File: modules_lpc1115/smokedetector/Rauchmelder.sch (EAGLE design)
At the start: 75 parts, among them IC1 BD9G101, IC2 LPC1115, Q1 BC856, Q3 BCP52, Q4 ASFL, T1 BC847C, T2 BC847C

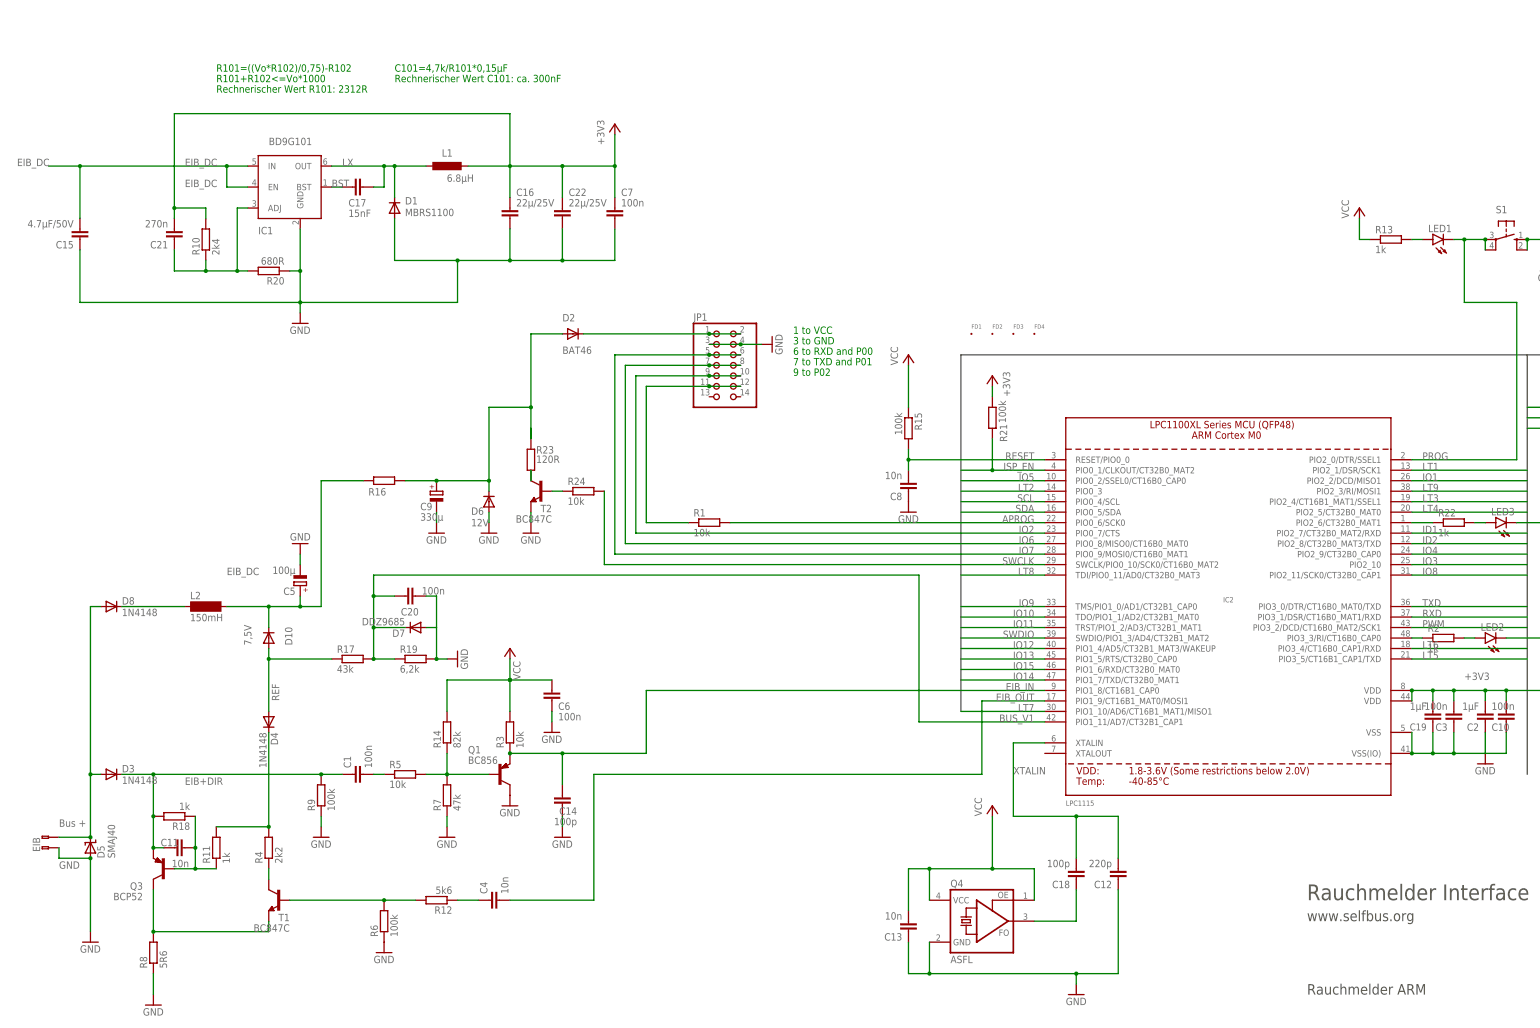
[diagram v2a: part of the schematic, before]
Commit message: [RM] - pwr mlccs changed to 2 x 47uF and adj-voltage divider 1k6/470R
- according to ROHM spec: switched to 2 x 47uF mlccs (instead of 1 x 22uF of the old design)
- according to ROHM spec: adjusted voltage divider to get 3,3V output instead of  (instead of  3,397V from the old design)
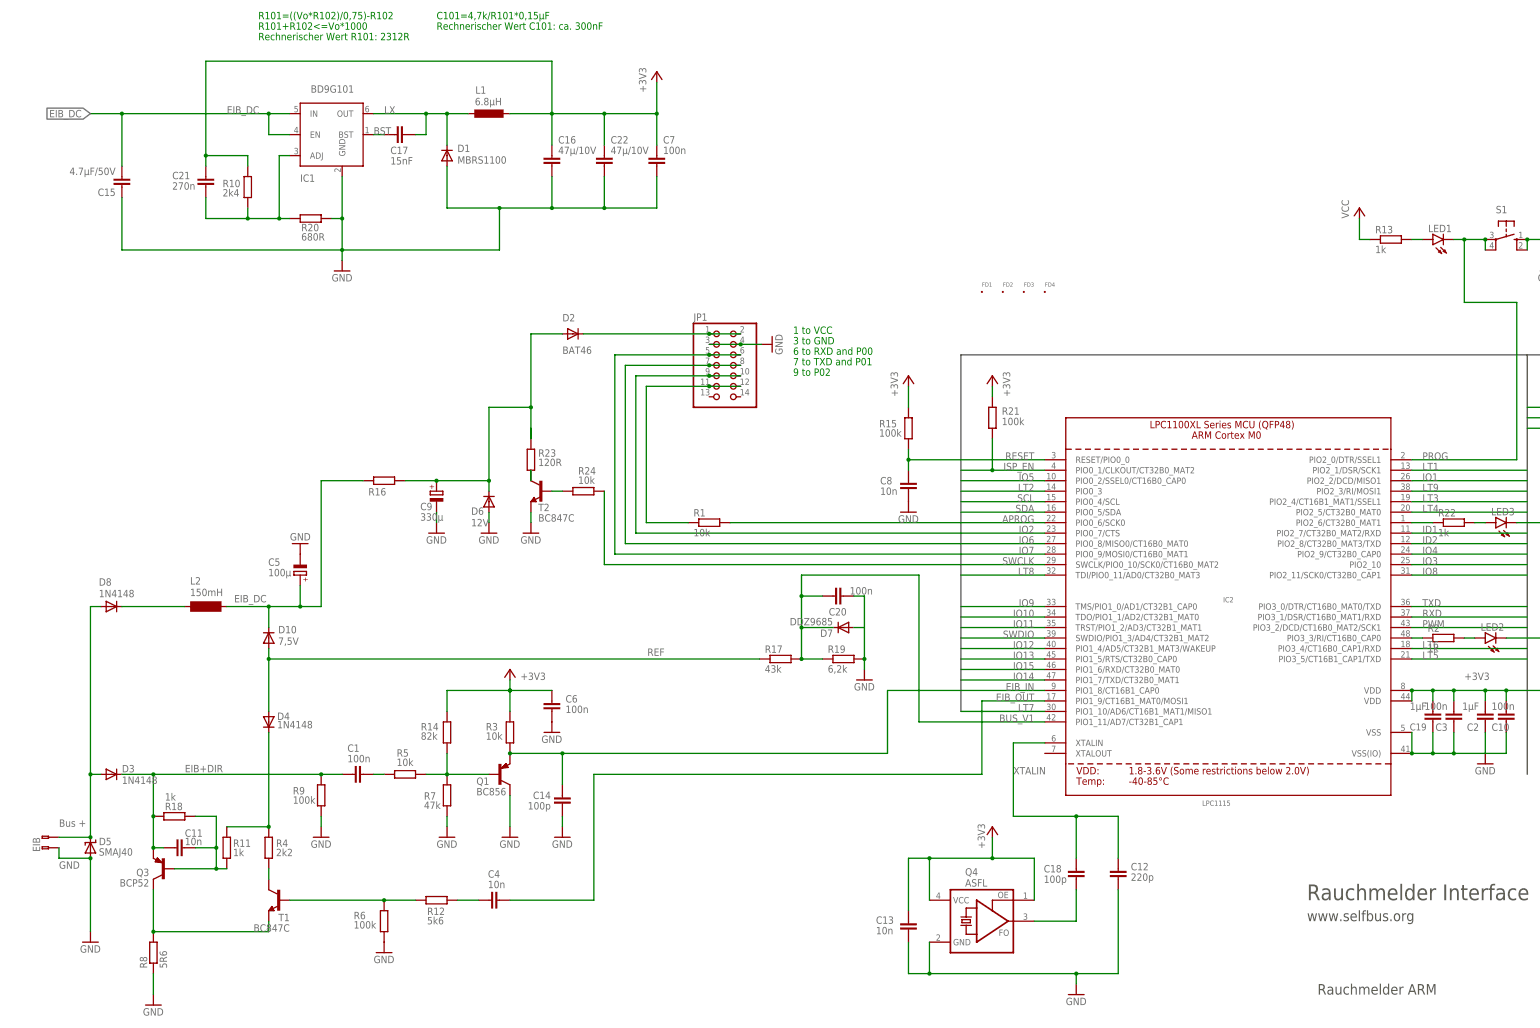
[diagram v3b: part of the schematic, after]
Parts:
- C16, C22: value 22µ/25V -> 47µ/10V
- D1: device microbuilder:DIODESMA -> microbuilder:DIODESOD-123
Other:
- moved on the sheet: C15, C16, C17, C20, C21, C22, C5, C6, C7, D1, D7, FD1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

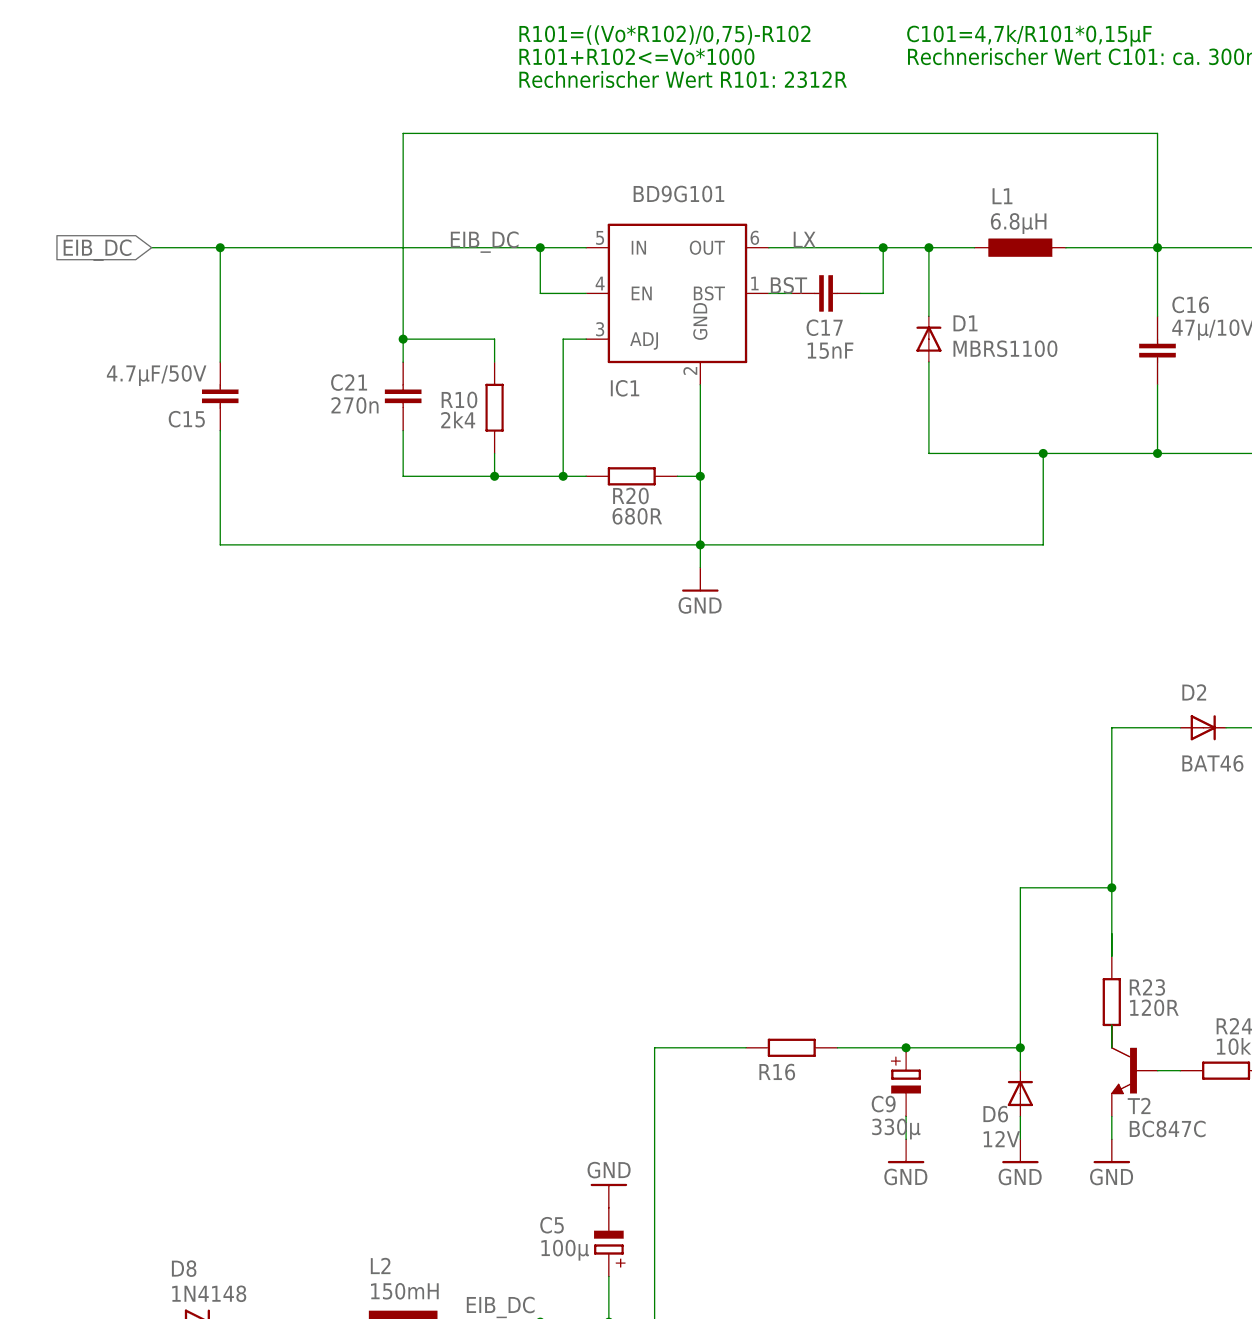
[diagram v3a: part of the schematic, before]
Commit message: [RM] - removed thermals from buck converter polygons
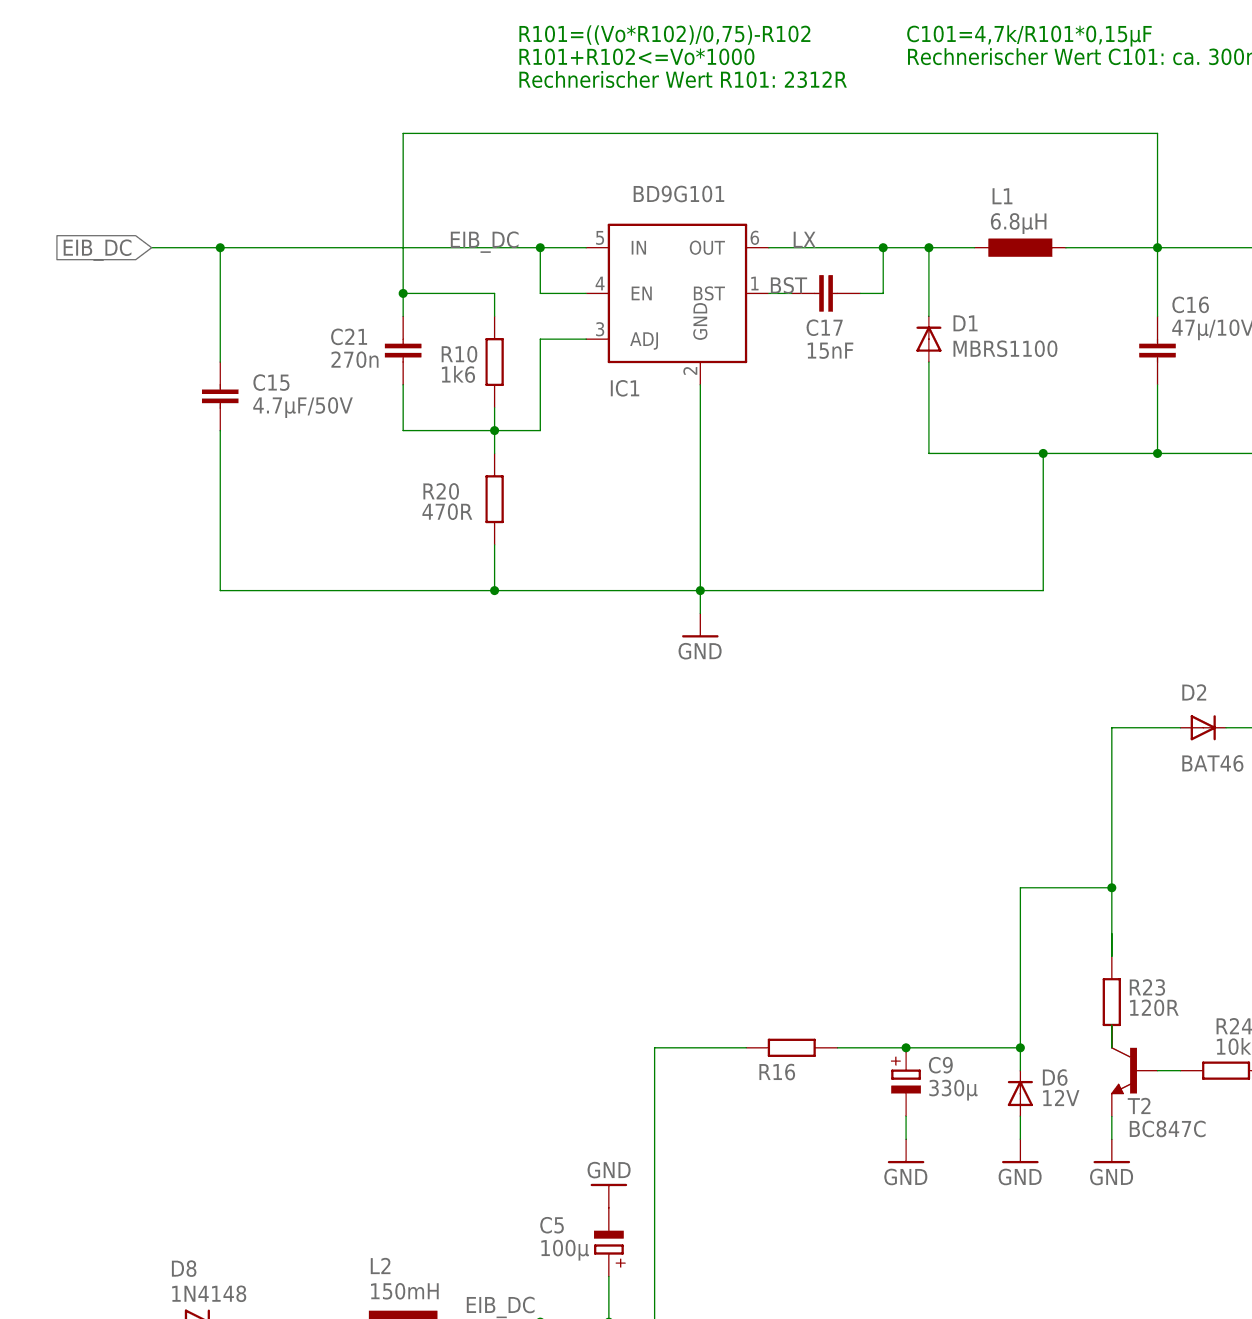
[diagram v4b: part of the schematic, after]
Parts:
- R10: value 2k4 -> 1k6
- R20: value 680R -> 470R
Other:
- moved on the sheet: C21, R10, R20

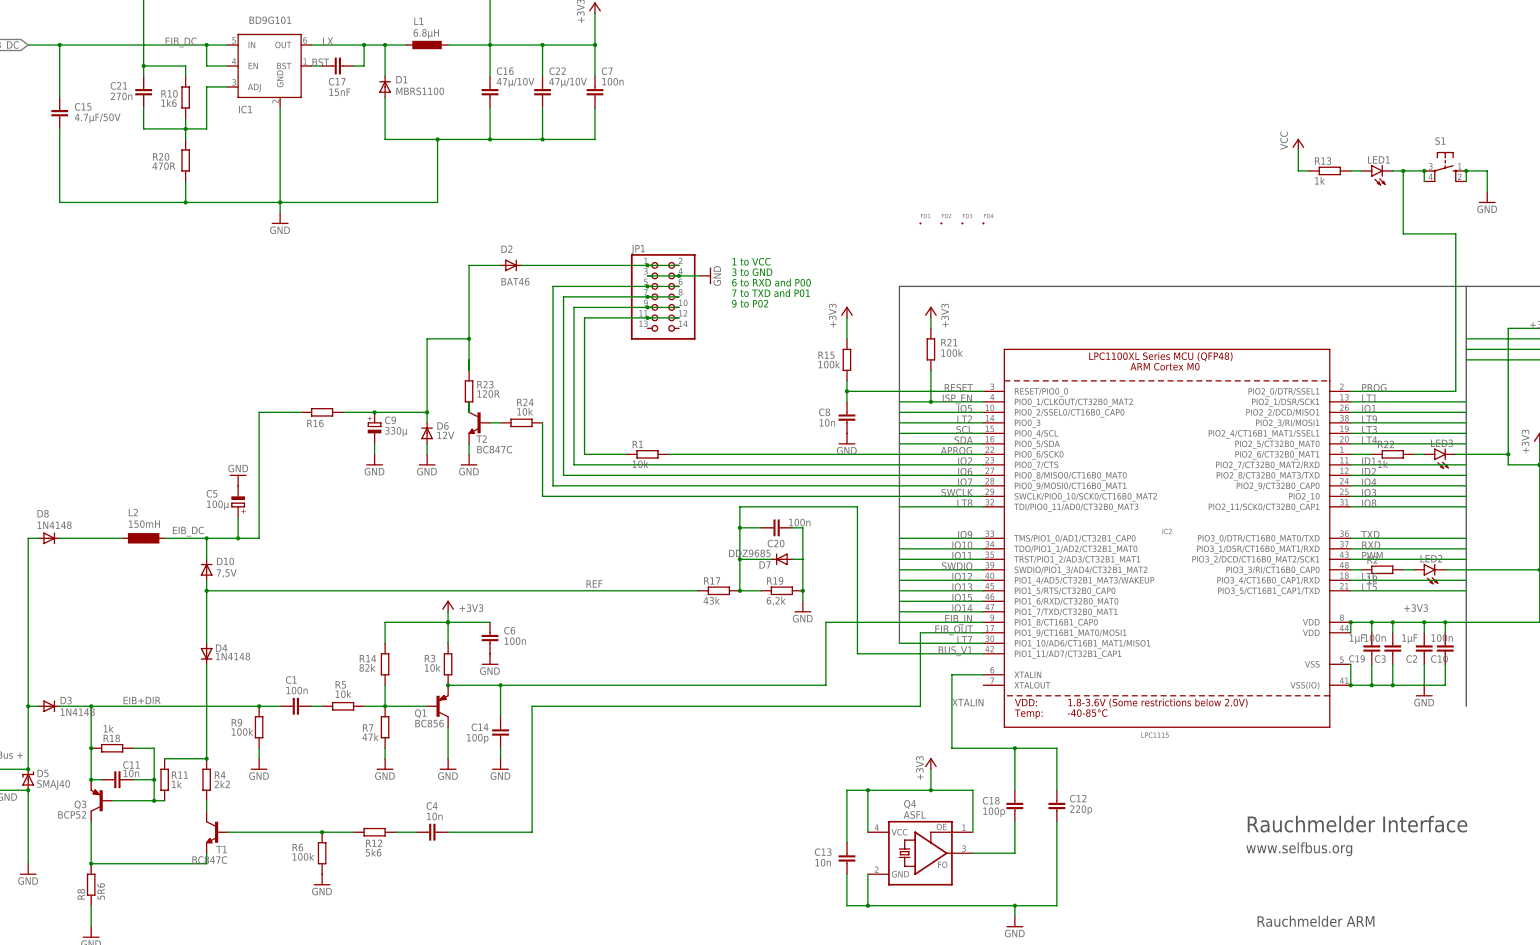
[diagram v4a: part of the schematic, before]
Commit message: [RM] - changed footprints from 1206 to 0805
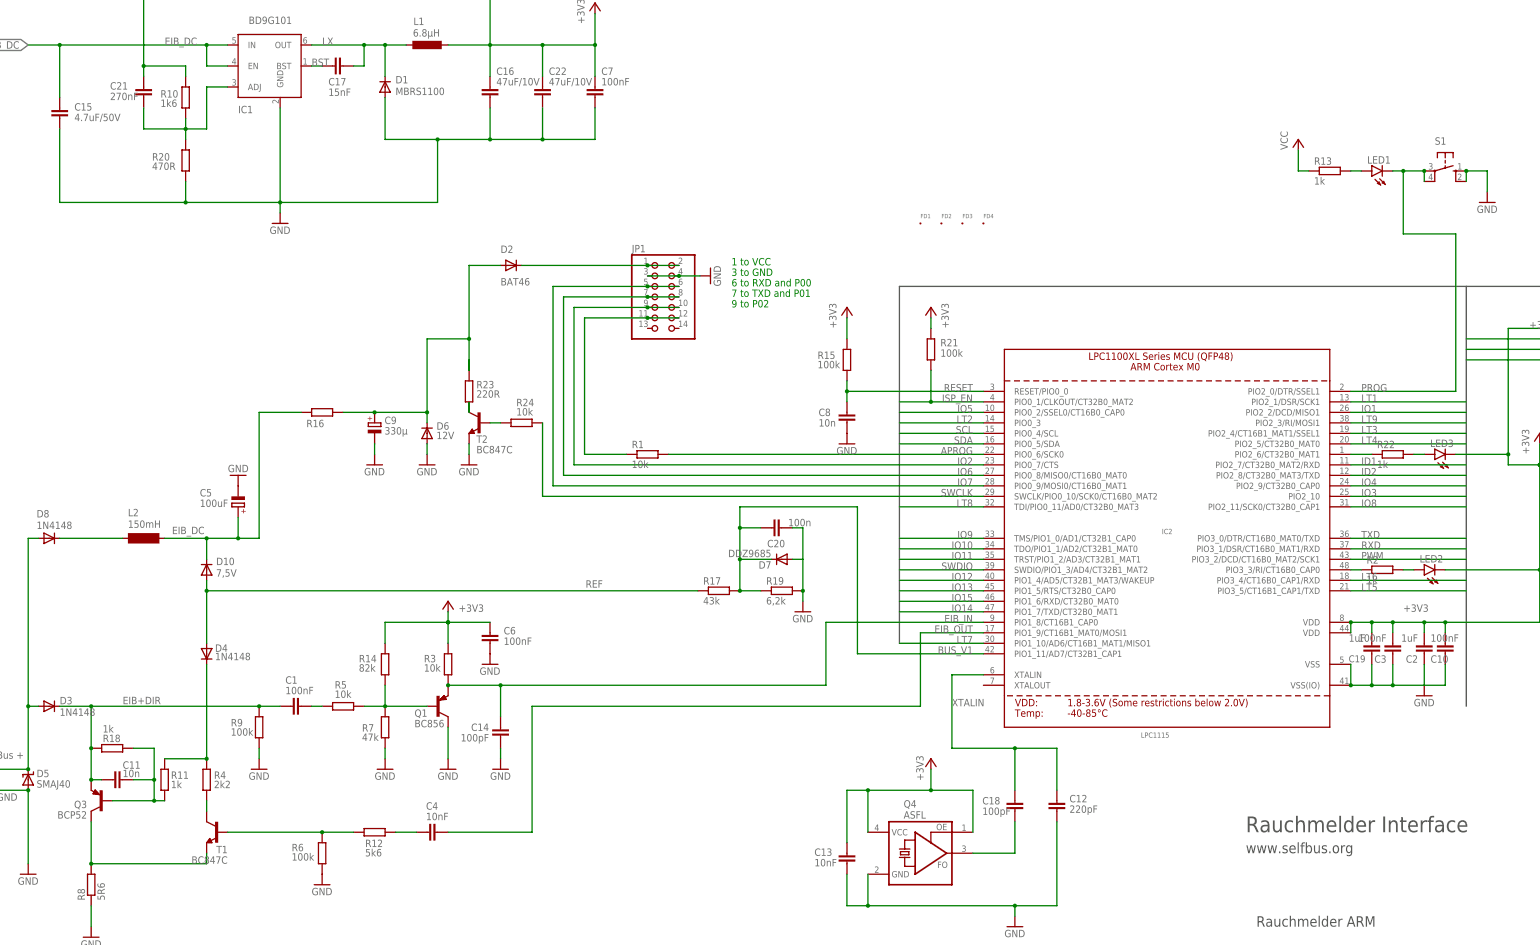
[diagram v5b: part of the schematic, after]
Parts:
- C1, C10, C3, C6, C7: value 100n -> 100nF; device rcl:C-EUC1206 -> rcl:C-EUC0805
- C11, C20, C8: device rcl:C-EUC1206 -> rcl:C-EUC0805
- C12: value 220p -> 220pF; device rcl:C-EUC1206 -> rcl:C-EUC0805
- C13, C4: value 10n -> 10nF; device rcl:C-EUC1206 -> rcl:C-EUC0805
- C14, C18: value 100p -> 100pF; device rcl:C-EUC1206 -> rcl:C-EUC0805
- C15: value 4.7µF/50V -> 4.7uF/50V; device rcl:C-EUC1206 -> rcl:C-EUC0805
- C16, C22: value 47µ/10V -> 47uF/10V; device rcl:C-EUC1206 -> rcl:C-EUC0805
- C19, C2: value 1µF -> 1uF; device rcl:C-EUC1206 -> rcl:C-EUC0805
- C21: value 270n -> 270nF; device rcl:C-EUC1206 -> rcl:C-EUC0805
- C5: value 100µ -> 100uF
- LED1, LED2, LED3: device led:LEDCHIPLED_1206 -> led:LEDCHIPLED_0805
- R1, R10, R11, R12, R13, R14, R15, R16, R17, R18, R19, R2, R20, R21, R22, R24, R3, R4, R5, R6, R7, R9: device rcl:R-EU_R1206 -> rcl:R-EU_R0805
- R23: value 120R -> 220R; device rcl:R-EU_R1206 -> rcl:R-EU_R2512
